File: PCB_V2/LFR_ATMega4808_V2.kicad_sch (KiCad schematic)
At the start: 72 parts, among them J1 Conn_02x02_Odd_Even, J2 Conn_02x05_Odd_Even, J3 Conn_02x02_Counter_Clockwise, J4 Conn_02x02_Counter_Clockwise, J5 Conn_02x02_Counter_Clockwise, J6 Conn_02x03_Odd_Even, J7 Conn_02x02_Odd_Even, Q1 PMOS, Q2 NMOS, Q3 NMOS, Q4 NMOS, Q5 NMOS, Q6 PMOS, Q7 NMOS, Q8 NMOS, U1 ATmega4808-A, U5 MCP1700x-330xxTO

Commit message: Rough layout done
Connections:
- net GND: now also C12.1
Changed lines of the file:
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@@
+	)
+	(symbol
+		(lib_id "power:GND")
+		(at 256.54 63.5 0)
+		(mirror y)
+		(unit 1)
+		(body_style 1)
+		(exclude_from_sim no)
+		(in_bom yes)
+		(on_board yes)
+		(in_pos_files yes)
+		(dnp no)
+		(fields_autoplaced yes)
+		(property "Reference" "#PWR061"
+			(at 256.54 69.85 0)
+			(hide yes)
+			(show_name no)
+			(do_not_autoplace no)
+			(effects
+				(font
+					(size 1.27 1.27)
+				)
+			)
+		)
+		(property "Value" "GND"
+			(at 256.54 68.58 0)
+			(hide yes)
+			(show_name no)
+			(do_not_autoplace no)
+			(effects
+				(font
+					(size 1.27 1.27)
+				)
+			)
+		)
+		(property "Footprint" ""
+			(at 256.54 63.5 0)
+			(hide yes)
+			(show_name no)
+			(do_not_autoplace no)
+			(effects
+				(font
+					(size 1.27 1.27)
+				)
+			)
+		)
+		(property "Datasheet" ""
+			(at 256.54 63.5 0)
+			(hide yes)
+			(show_name no)
+			(do_not_autoplace no)
+			(effects
+				(font
+					(size 1.27 1.27)
+				)
+			)
+		)
+		(property "Description" "Power symbol creates a global label with name \"GND\" , ground"
+			(at 256.54 63.5 0)
+			(hide yes)
+			(show_name no)
+			(do_not_autoplace no)
+			(effects
+				(font
+					(size 1.27 1.27)
+				)
+			)
+		)
+		(pin "1"
+		)
+		(instances
+			(project "LFR_ATMega4808_V2"
+				(path "/7fcd8b9a-e9e6-4d51-9258-8399f733a0d2"
+					(reference "#PWR061")
+					(unit 1)
+				)
+			)
+		)
 	)
 	(symbol

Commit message: Everything except for buttons is done
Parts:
- S2, S4: footprint MJTP1230:SW_MJTP1230 -> MJTP1230_:Switch_Tactile_THT_6x6mm_MJTP1230
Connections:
- net Brake 1: now also U1.9 (PC3); no longer U1.32 (PA2)
- net Brake 2: now also U1.32 (PA2); no longer U1.9 (PC3)
- net Motor 1: now also U1.4 (PA6); no longer U1.1 (PA3)
- net Motor 2: now also U1.5 (PA7); no longer U1.2 (PA4)
- net Motor 3: now also U1.2 (PA4); no longer U1.4 (PA6)
- net Motor 4: now also U1.1 (PA3); no longer U1.5 (PA7)
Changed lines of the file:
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@@
 	(global_label "Motor 3"
 		(shape input)
-		(at 64.77 53.34 0)
+		(at 64.77 48.26 0)
 		(fields_autoplaced yes)
 		(effects
@@
 		)
 		(property "Intersheetrefs" "${INTERSHEET_REFS}"
-			(at 75.1936 53.34 0)
+			(at 75.1936 48.26 0)
 			(hide yes)
 			(show_name no)
@@
 	(global_label "Motor 4"
 		(shape input)
-		(at 64.77 55.88 0)
+		(at 64.77 45.72 0)
 		(fields_autoplaced yes)
 		(effects
@@
 		)
 		(property "Intersheetrefs" "${INTERSHEET_REFS}"
-			(at 75.1936 55.88 0)
+			(at 75.1936 45.72 0)
 			(hide yes)
 			(show_name no)
@@
 	(global_label "Motor 1"
 		(shape input)
-		(at 64.77 45.72 0)
+		(at 64.77 53.34 0)
 		(fields_autoplaced yes)
 		(effects
@@
 		)
 		(property "Intersheetrefs" "${INTERSHEET_REFS}"
-			(at 75.1936 45.72 0)
+			(at 75.1936 53.34 0)
 			(hide yes)
 			(show_name no)
@@
 	(global_label "Brake 1"
 		(shape input)
-		(at 64.77 43.18 0)
+		(at 64.77 68.58 0)
 		(fields_autoplaced yes)
 		(effects
@@
 		)
 		(property "Intersheetrefs" "${INTERSHEET_REFS}"
-			(at 75.2542 43.18 0)
+			(at 75.2542 68.58 0)
 			(hide yes)
 			(show_name no)
@@
 	(global_label "Motor 2"
 		(shape input)
-		(at 64.77 48.26 0)
+		(at 64.77 55.88 0)
 		(fields_autoplaced yes)
 		(effects
@@
 		)
 		(property "Intersheetrefs" "${INTERSHEET_REFS}"
-			(at 75.1936 48.26 0)
+			(at 75.1936 55.88 0)
 			(hide yes)
 			(show_name no)
@@
 	(global_label "Brake 2"
 		(shape input)
-		(at 64.77 68.58 0)
+		(at 64.77 43.18 0)
 		(fields_autoplaced yes)
 		(effects
@@
 		)
 		(property "Intersheetrefs" "${INTERSHEET_REFS}"
-			(at 75.2542 68.58 0)
+			(at 75.2542 43.18 0)
 			(hide yes)
 			(show_name no)
@@
 			)
 		)
-		(property "Footprint" "MJTP1230:SW_MJTP1230"
+		(property "Footprint" "MJTP1230_:Switch_Tactile_THT_6x6mm_MJTP1230"
 			(at 39.37 167.64 0)
 			(hide yes)
@@
 			)
 		)
-		(property "Footprint" "MJTP1230:SW_MJTP1230"
+		(property "Footprint" "MJTP1230_:Switch_Tactile_THT_6x6mm_MJTP1230"
 			(at 133.35 38.1 0)
 			(hide yes)

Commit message: Finished the wiring, now on to the silkscreen
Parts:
- H1, H2, H3, H4: footprint MountingHole:MountingHole_2.2mm_M2 -> MountingHole:MountingHole_2.2mm_M2_Pad
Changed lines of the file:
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@@
 			)
 		)
-		(property "Footprint" "MountingHole:MountingHole_2.2mm_M2"
+		(property "Footprint" "MountingHole:MountingHole_2.2mm_M2_Pad"
 			(at 88.9 101.6 0)
 			(hide yes)
@@
 			)
 		)
-		(property "Footprint" "MountingHole:MountingHole_2.2mm_M2"
+		(property "Footprint" "MountingHole:MountingHole_2.2mm_M2_Pad"
 			(at 88.9 86.36 0)
 			(hide yes)
@@
 			)
 		)
-		(property "Footprint" "MountingHole:MountingHole_2.2mm_M2"
+		(property "Footprint" "MountingHole:MountingHole_2.2mm_M2_Pad"
 			(at 88.9 96.52 0)
 			(hide yes)
@@
 			)
 		)
-		(property "Footprint" "MountingHole:MountingHole_2.2mm_M2"
+		(property "Footprint" "MountingHole:MountingHole_2.2mm_M2_Pad"
 			(at 88.9 91.44 0)
 			(hide yes)

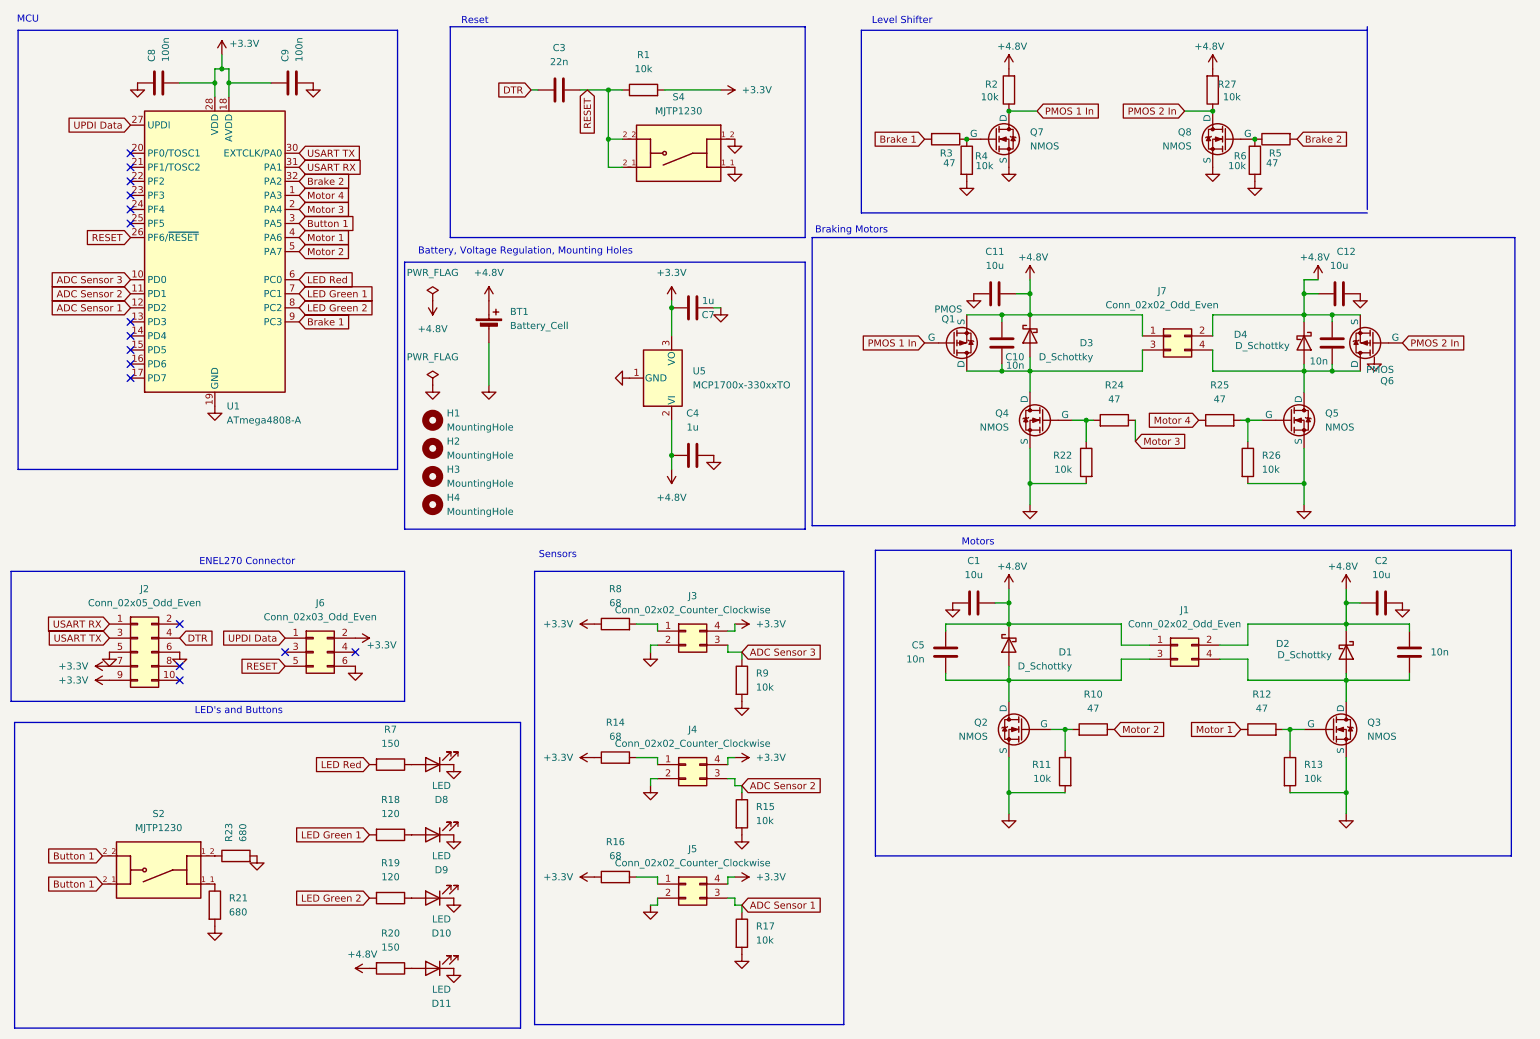
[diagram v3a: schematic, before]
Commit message: Changed sensors to take input from a separate PCB
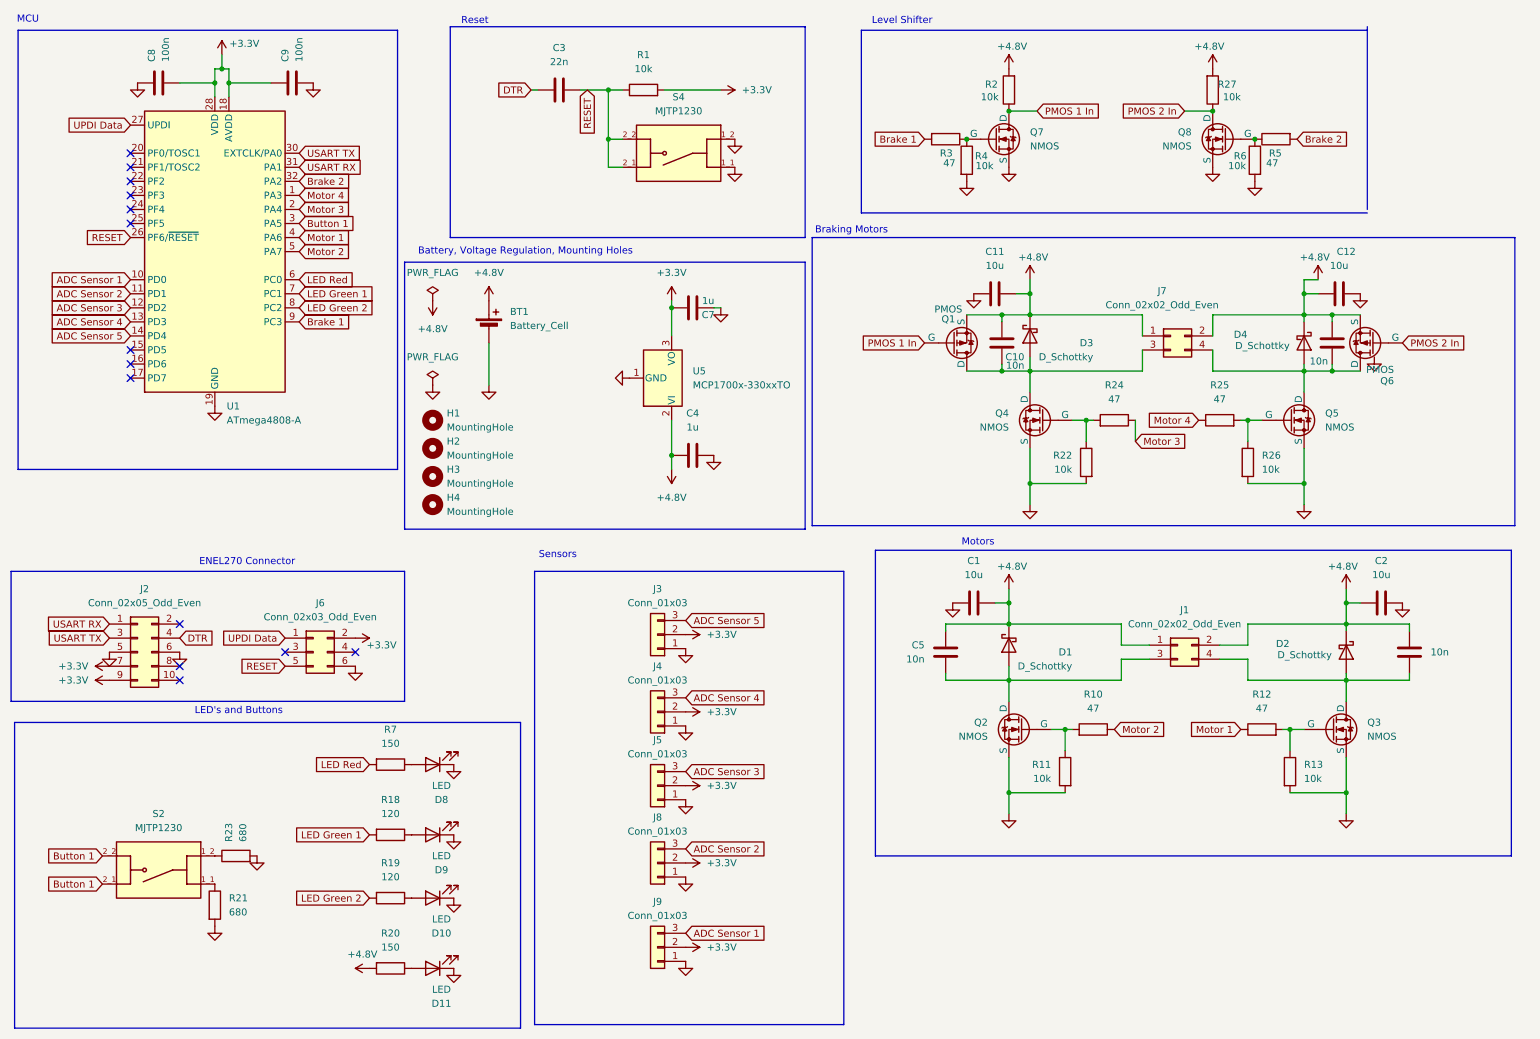
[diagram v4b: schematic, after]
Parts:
- removed J3, J4, J5: Conn_02x02_Counter_Clockwise, Connector_PinHeader_2.54mm:PinHeader_2x02_P2.54mm_Vertical, symbol Connector_Generic:Conn_02x02_Counter_Clockwise
- removed R14, R16, R8: 68, Resistor_SMD:R_0805_2012Metric_Pad1.20x1.40mm_HandSolder, symbol Device:R
- removed R15, R17, R9: 10k, Resistor_SMD:R_0805_2012Metric_Pad1.20x1.40mm_HandSolder, symbol Device:R
- added J3, J4, J5, J8, J9: Conn_01x03, Connector_PinHeader_2.54mm:PinHeader_1x03_P2.54mm_Vertical, symbol Connector_Generic:Conn_01x03
- BT1: footprint Connector_PinSocket_1.00mm:PinSocket_1x02_P1.00mm_Vertical_SMD_Pin1Left -> Connector_PinHeader_2.54mm:PinHeader_1x02_P2.54mm_Vertical
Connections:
- net +3.3V: now also J3.2 (Pin_2), J4.2 (Pin_2), J5.2 (Pin_2), J8.2 (Pin_2), J9.2 (Pin_2)
- net ADC Sensor 1: now also U1.10 (PD0), J9.3 (Pin_3); no longer U1.12 (PD2)
- net ADC Sensor 2: now also J8.3 (Pin_3)
- net ADC Sensor 3: now also U1.12 (PD2), J5.3 (Pin_3); no longer U1.10 (PD0)
- net GND: now also J3.1 (Pin_1), J4.1 (Pin_1), J5.1 (Pin_1), J8.1 (Pin_1), J9.1 (Pin_1)
- net ADC Sensor 4: now reaches U1.13 (PD3)
- net ADC Sensor 4: now also J4.3 (Pin_3)
- net ADC Sensor 5: now reaches U1.14 (PD4)
- net ADC Sensor 5: now also J3.3 (Pin_3)
- no-connect marks 16 -> 14

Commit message: Added test points
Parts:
- removed J3, J4: Conn_01x03, Connector_PinHeader_2.54mm:PinHeader_1x03_P2.54mm_Vertical, symbol Connector_Generic:Conn_01x03
- added J10, J11: Conn_01x03, Connector_PinHeader_2.54mm:PinHeader_1x03_P2.54mm_Vertical, symbol Connector_Generic:Conn_01x03
- added TP1, TP2, TP3, TP4, TP5, TP6: TestPoint, TestPoint:TestPoint_Pad_D1.0mm, symbol Connector:TestPoint
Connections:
- net +3.3V: now also J10.2 (Pin_2), J11.2 (Pin_2), TP1.1
- net +4.8V: now also TP2.1
- net ADC Sensor 4: now also J10.3 (Pin_3)
- net ADC Sensor 5: now also J11.3 (Pin_3)
- net GND: now also J10.1 (Pin_1), J11.1 (Pin_1)
- net at C10.2, D3.2 (A), J7.3 (Pin_3)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: now also TP6.1
- net at C5.2, D1.2 (A), J1.3 (Pin_3)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: now also TP3.1
- net at C13.2, D4.2 (A), J7.4 (Pin_4)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: now also TP5.1
- net at C6.2, D2.2 (A), J1.4 (Pin_4)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: now also TP4.1

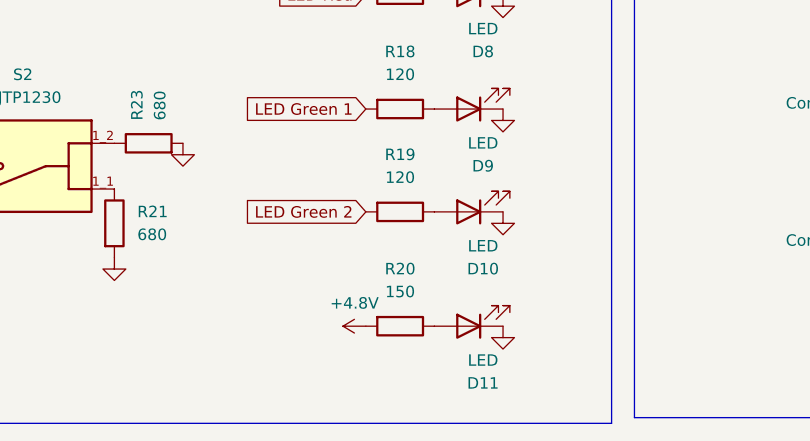
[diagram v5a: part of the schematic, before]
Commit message: Board reviewed with AI, changed Blue LED R Value
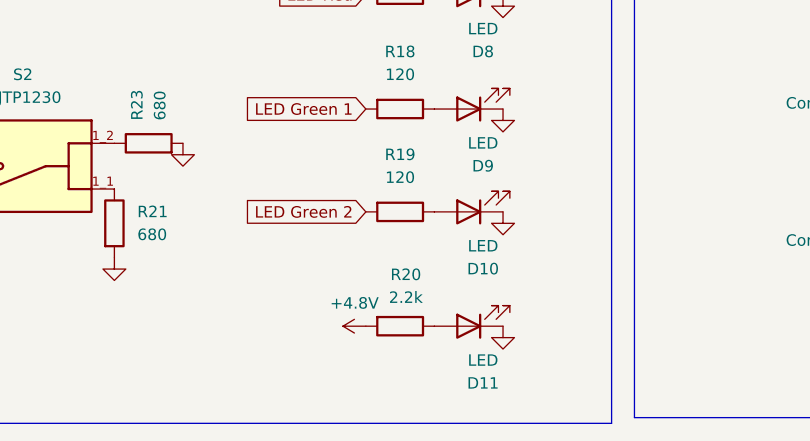
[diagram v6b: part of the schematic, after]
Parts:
- R20: value 150 -> 2.2k
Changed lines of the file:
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@@
 		(in_pos_files yes)
 		(dnp no)
-		(fields_autoplaced yes)
 		(property "Reference" "R20"
-			(at 81.28 179.07 90)
+			(at 81.915 179.705 90)
 			(show_name no)
 			(do_not_autoplace no)
@@
 			)
 		)
-		(property "Value" "150"
-			(at 81.28 181.61 90)
+		(property "Value" "2.2k"
+			(at 81.915 182.245 90)
 			(show_name no)
 			(do_not_autoplace no)

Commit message: The transistor pins were wrong. Everything is adjusted and rewired
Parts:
- removed Q1, Q6: PMOS, Package_TO_SOT_SMD:SOT-23-3, symbol Simulation_SPICE:PMOS
- removed Q2, Q3, Q4, Q5, Q7, Q8: NMOS, Package_TO_SOT_SMD:SOT-23, symbol Simulation_SPICE:NMOS
- added Q1: PMOS_Si2333DDS, Package_TO_SOT_SMD:SOT-23-3, symbol Local_FETS:PMOS_Si2333DDS
- added Q10, Q11, Q5, Q6, Q7, Q8: NMOS_BSR802NL6327HTSA1, Package_TO_SOT_SMD:SOT-23-3, symbol Local_FETS:NMOS_BSR802NL6327HTSA1
- added Q9: PMOS_Si2333DDS, Package_TO_SOT_SMD:SOT-23, symbol Local_FETS:PMOS_Si2333DDS
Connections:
- net +4.8V: now also Q1.2 (S), Q9.2 (S)
- net GND: now also Q10.2 (S), Q11.2 (S), Q5.2 (S), Q6.2 (S), Q7.2 (S), Q8.2 (S)
- net PMOS 1 In: now also Q1.1 (G), Q7.3 (D)
- net PMOS 2 In: now also Q8.3 (D), Q9.1 (G)
- net at R22.1, R24.2: now also Q6.1 (G)
- net at R3.1, R4.1: now also Q7.1 (G)
- net at R5.1, R6.1: now also Q8.1 (G)
- net at C10.2, D3.2 (A), J7.3 (Pin_3)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: now also Q1.3 (D), Q6.3 (D)
- net at C5.2, D1.2 (A), J1.3 (Pin_3)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: now also Q11.3 (D)
- net at C6.2, D2.2 (A), J1.4 (Pin_4)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: now also Q10.3 (D)
- net at C13.2, D4.2 (A), J7.4 (Pin_4)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: now also Q5.3 (D), Q9.3 (D)
- net at R12.2, R13.1: now also Q10.1 (G)
- net at R25.2, R26.1: now also Q5.1 (G)
- net at R10.2, R11.1: now also Q11.1 (G)
